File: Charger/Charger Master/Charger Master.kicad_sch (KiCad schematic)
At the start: 0 parts

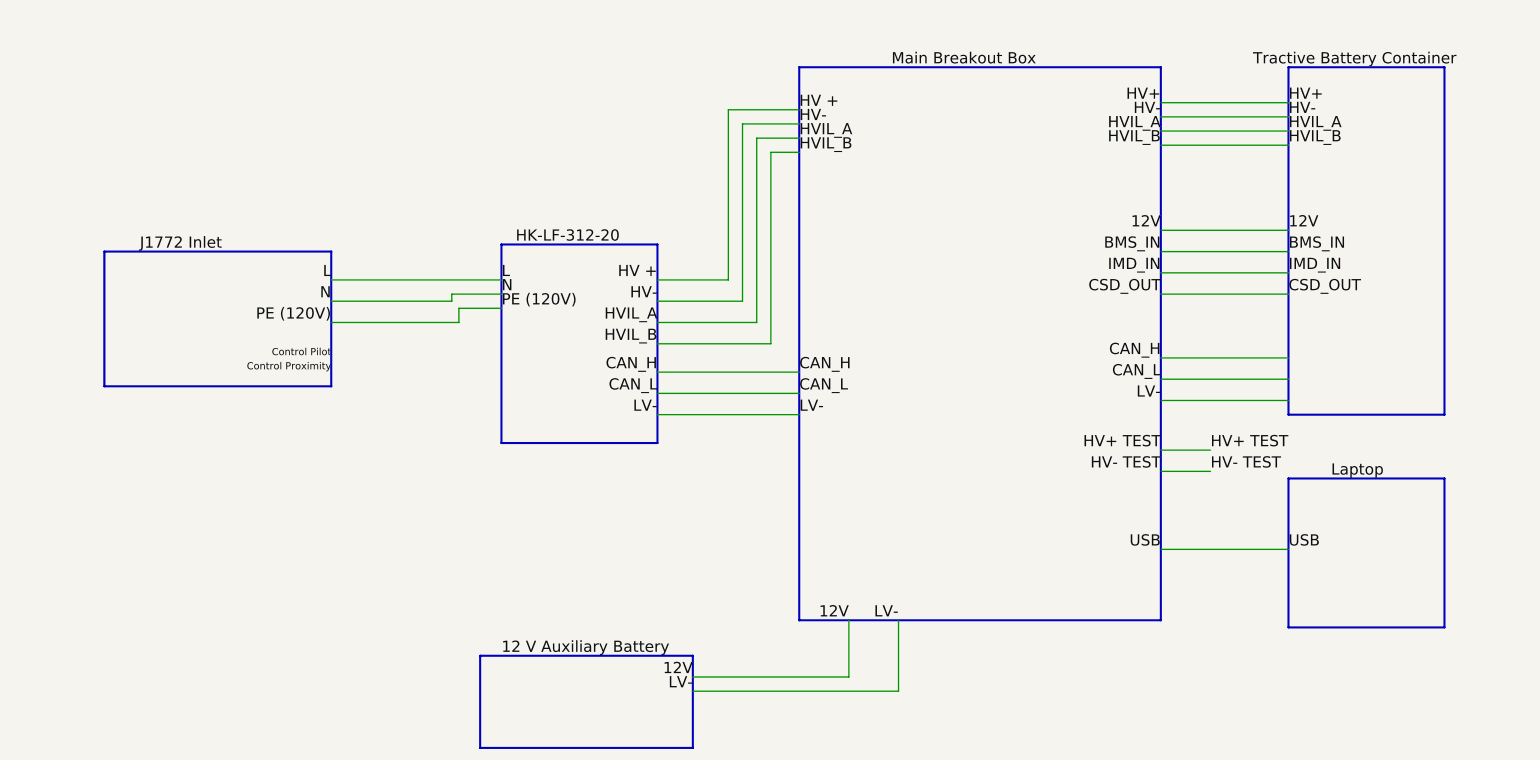
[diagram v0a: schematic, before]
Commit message: Started implementing hierarchial sheets
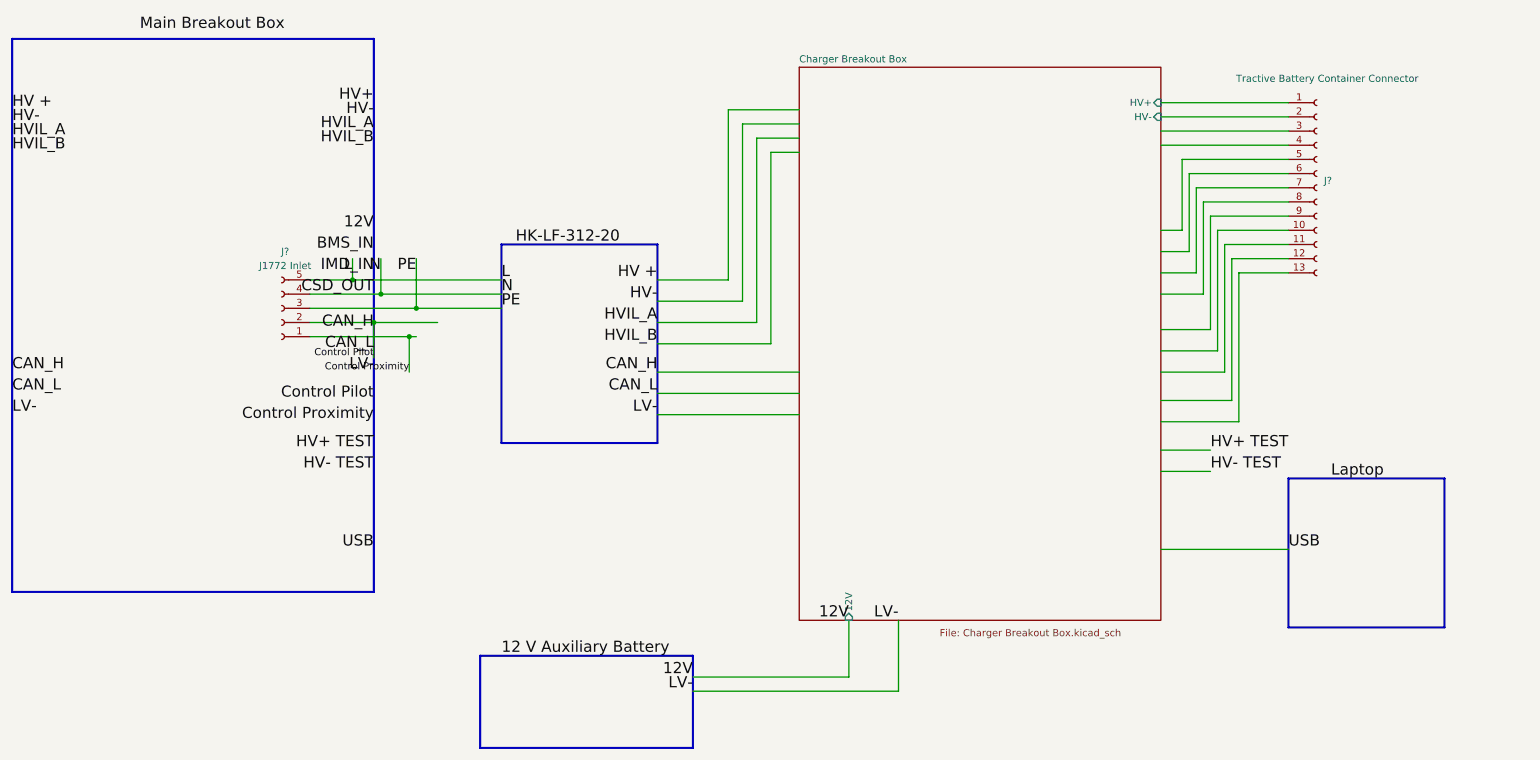
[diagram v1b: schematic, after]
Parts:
- added J?: Tractive Battery Container Connector, symbol Connector:Conn_01x13_Socket
- added J?: J1772 Inlet, symbol Connector:Conn_01x05_Socket
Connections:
- net CAN_H: now also J?.2 (Pin_2)
- net CSD_OUT: now also J?.4 (Pin_4)
- net Control Proximity: now also J?.1 (Pin_1)
- net L: now also J?.5 (Pin_5)
- new net Charger Breakout Box/HV+: J?.1 (Pin_1)
- new net Charger Breakout Box/HV-: J?.2 (Pin_2)
- new net PE: J?.3 (Pin_3)
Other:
- added sheet Charger Breakout Box (Charger Breakout Box.kicad_sch)
